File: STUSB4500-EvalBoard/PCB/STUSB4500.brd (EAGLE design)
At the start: 16 x 26 mm, 25 parts

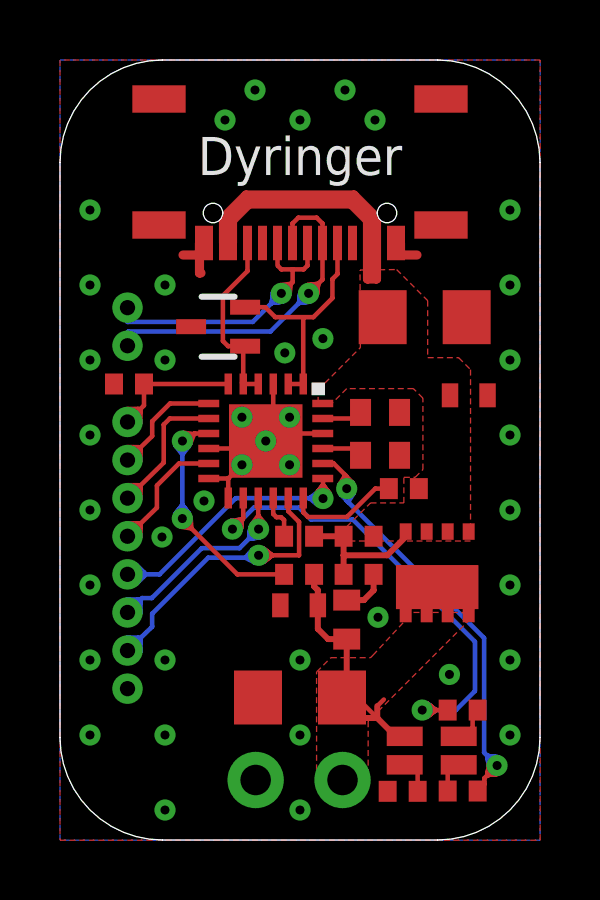
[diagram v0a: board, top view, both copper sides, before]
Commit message: Fixed isolation value on top layer
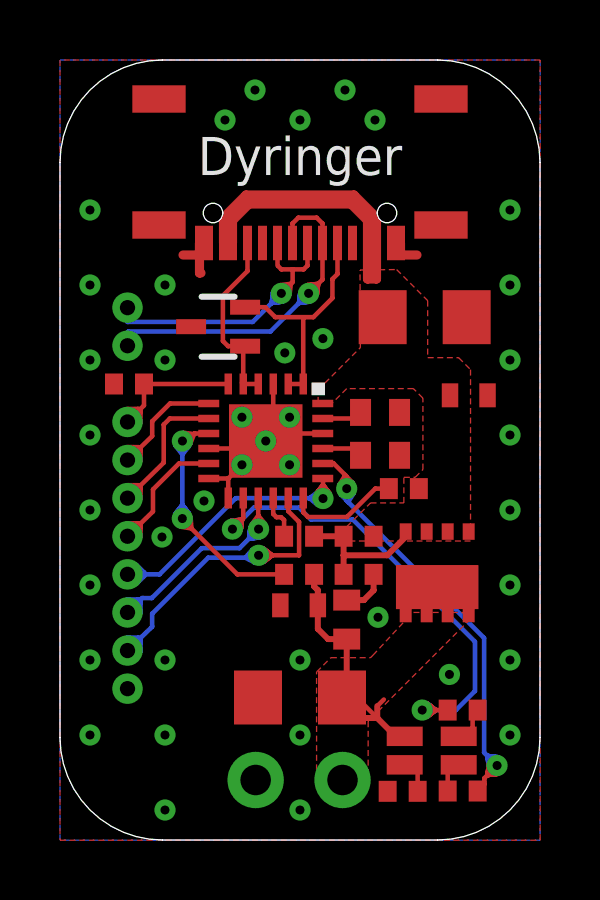
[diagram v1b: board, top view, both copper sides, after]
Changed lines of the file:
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@@
 <wire x1="7.232290625" y1="13.55" x2="7.108125" y2="13.55" width="0.1524" layer="1"/>
 <wire x1="7.108125" y1="15.2" x2="7.108125" y2="13.67416875" width="0.1524" layer="1"/>
-<polygon width="0.1524" layer="1" isolate="0.254" rank="2">
+<polygon width="0.1524" layer="1" isolate="0.1" rank="2">
 <vertex x="0" y="26"/>
 <vertex x="0" y="-0.0075"/>
@@
 <wire x1="7.108125" y1="13.674165625" x2="7.134365625" y2="13.32049375" width="0.1524" layer="1"/>
 <wire x1="6.858125" y1="13.3" x2="7.134365625" y2="13.32049375" width="0.1524" layer="1"/>
-<wire x1="10.5" y1="24" x2="12.7" y2="24.7" width="0" layer="19" extent="1-1"/>
-<wire x1="9.5" y1="25" x2="10.5" y2="24" width="0" layer="19" extent="1-1"/>
-<wire x1="8" y1="24" x2="9.5" y2="25" width="0" layer="19" extent="1-1"/>
-<wire x1="6.5" y1="25" x2="8" y2="24" width="0" layer="19" extent="1-1"/>
-<wire x1="5.5" y1="24" x2="6.5" y2="25" width="0" layer="19" extent="1-1"/>
-<wire x1="3.3" y1="24.7" x2="5.5" y2="24" width="0" layer="19" extent="1-1"/>
-<wire x1="12.7" y1="20.5" x2="10.5" y2="24" width="0" layer="19" extent="1-1"/>
-<wire x1="11.9" y1="19.5" x2="12.7" y2="20.5" width="0" layer="19" extent="1-1"/>
-<wire x1="15" y1="21" x2="12.7" y2="20.5" width="0" layer="19" extent="1-1"/>
-<wire x1="15" y1="18.5" x2="15" y2="21" width="0" layer="19" extent="1-1"/>
-<wire x1="13.555625" y1="17.4275" x2="15" y2="18.5" width="0" layer="19" extent="1-1"/>
-<wire x1="15" y1="16" x2="13.555625" y2="17.4275" width="0" layer="19" extent="1-1"/>
-<wire x1="14.250625" y1="14.8225" x2="15" y2="16" width="0" layer="19" extent="1-1"/>
-<wire x1="15" y1="13.5" x2="14.250625" y2="14.8225" width="0" layer="19" extent="1-1"/>
-<wire x1="15" y1="11" x2="15" y2="13.5" width="0" layer="19" extent="1-1"/>
-<wire x1="15" y1="8.5" x2="15" y2="11" width="0" layer="19" extent="1-1"/>
-<wire x1="15" y1="6" x2="15" y2="8.5" width="0" layer="19" extent="1-1"/>
-<wire x1="12.98125" y1="5.51875" x2="15" y2="6" width="0" layer="19" extent="1-1"/>
-<wire x1="15" y1="3.5" x2="15" y2="6" width="0" layer="19" extent="1-1"/>
-<wire x1="11.318125" y1="14.2525" x2="14.250625" y2="14.8225" width="0" layer="19" extent="1-1"/>
-<wire x1="11.318125" y1="12.82375" x2="11.318125" y2="14.2525" width="0" layer="19" extent="1-1"/>
-<wire x1="8.758125" y1="13.55" x2="11.318125" y2="14.2525" width="0" layer="19" extent="1-1"/>
-<wire x1="6.223125" y1="12.9825" x2="6.608125" y2="13.05" width="0" layer="19" extent="1-1"/>
-<wire x1="6.064375" y1="12.50625" x2="6.223125" y2="12.9825" width="0" layer="19" extent="1-1"/>
-<wire x1="4.8" y1="11.3" x2="4.958125" y2="12.05" width="0" layer="19" extent="1-1"/>
-<wire x1="7.493125" y1="16.236875" x2="7.108125" y2="15.2" width="0" layer="19" extent="1-1"/>
-<wire x1="7.651875" y1="14.09375" x2="6.858125" y2="13.3" width="0" layer="19" extent="1-1"/>
-<wire x1="6.064375" y1="14.09375" x2="6.858125" y2="13.3" width="0" layer="19" extent="1-1"/>
-<wire x1="7.651875" y1="12.50625" x2="6.858125" y2="13.3" width="0" layer="19" extent="1-1"/>
-<wire x1="8.763125" y1="16.713125" x2="7.493125" y2="16.236875" width="0" layer="19" extent="1-1"/>
-<wire x1="3.4" y1="10.1" x2="4.8" y2="11.3" width="0" layer="19" extent="1-1"/>
-<wire x1="1" y1="11" x2="3.4" y2="10.1" width="0" layer="19" extent="1-1"/>
-<wire x1="1" y1="13.5" x2="1" y2="11" width="0" layer="19" extent="1-1"/>
-<wire x1="1.8" y1="15.2" x2="1" y2="13.5" width="0" layer="19" extent="1-1"/>
-<wire x1="1" y1="16" x2="1.8" y2="15.2" width="0" layer="19" extent="1-1"/>
-<wire x1="3.5" y1="16" x2="1.8" y2="15.2" width="0" layer="19" extent="1-1"/>
-<wire x1="4.370625" y1="17.11" x2="3.5" y2="16" width="0" layer="19" extent="1-1"/>
-<wire x1="3.5" y1="18.5" x2="4.370625" y2="17.11" width="0" layer="19" extent="1-1"/>
-<wire x1="4.1" y1="19.5" x2="3.5" y2="18.5" width="0" layer="19" extent="1-1"/>
-<wire x1="3.3" y1="20.5" x2="4.1" y2="19.5" width="0" layer="19" extent="1-1"/>
-<wire x1="1" y1="21" x2="3.3" y2="20.5" width="0" layer="19" extent="1-1"/>
-<wire x1="1" y1="18.5" x2="1" y2="16" width="0" layer="19" extent="1-1"/>
-<wire x1="1" y1="8.5" x2="1" y2="11" width="0" layer="19" extent="1-1"/>
-<wire x1="1" y1="6" x2="1" y2="8.5" width="0" layer="19" extent="1-1"/>
-<wire x1="2.25" y1="5.045" x2="1" y2="6" width="0" layer="19" extent="1-1"/>
-<wire x1="3.5" y1="6" x2="2.25" y2="5.045" width="0" layer="19" extent="1-1"/>
-<wire x1="3.5" y1="3.5" x2="2.25" y2="5.045" width="0" layer="19" extent="1-1"/>
-<wire x1="1" y1="3.5" x2="2.25" y2="5.045" width="0" layer="19" extent="1-1"/>
-<wire x1="3.5" y1="1" x2="3.5" y2="3.5" width="0" layer="19" extent="1-1"/>
-<wire x1="10.6" y1="7.42375" x2="12.98125" y2="5.51875" width="0" layer="19" extent="1-1"/>
-<wire x1="8" y1="6" x2="10.6" y2="7.42375" width="0" layer="19" extent="1-1"/>
-<wire x1="6.6" y1="4.75" x2="8" y2="6" width="0" layer="19" extent="1-1"/>
-<wire x1="8" y1="3.5" x2="6.6" y2="4.75" width="0" layer="19" extent="1-1"/>
-<wire x1="7.344375" y1="7.823125" x2="8" y2="6" width="0" layer="19" extent="1-1"/>
-<wire x1="6.521575" y1="2" x2="8" y2="3.5" width="0" layer="19" extent="1-1"/>
-<wire x1="8" y1="1" x2="6.521575" y2="2" width="0" layer="19" extent="1-1"/>
-<wire x1="10.921875" y1="1.6225" x2="8" y2="1" width="0" layer="19" extent="1-1"/>
+<wire x1="6.608125" y1="13.05" x2="6.223125" y2="12.9825" width="0" layer="19" extent="1-1"/>
 </signal>
 <signal name="STUSB_RST">
@@
 <wire x1="10.55" y1="18.7" x2="10.55" y2="19.9" width="0.3048" layer="1"/>
 <wire x1="10.25" y1="18.7" x2="10.55" y2="18.7" width="0.3048" layer="1"/>
-<wire x1="11.961875" y1="11.7125" x2="13.000625" y2="14.8225" width="0" layer="19" extent="1-1"/>
-<wire x1="12.223125" y1="10.28125" x2="11.961875" y2="11.7125" width="0" layer="19" extent="1-1"/>
-<wire x1="12.923125" y1="10.28125" x2="12.223125" y2="10.28125" width="0" layer="19" extent="1-1"/>
-<wire x1="13.623125" y1="10.28125" x2="12.923125" y2="10.28125" width="0" layer="19" extent="1-1"/>
-<wire x1="10.45375" y1="10.125" x2="12.223125" y2="10.28125" width="0" layer="19" extent="1-1"/>
-<wire x1="10.755625" y1="17.4275" x2="13.000625" y2="14.8225" width="0" layer="19" extent="1-1"/>
-<wire x1="10.25" y1="19.9" x2="10.419375" y2="17.4275" width="0" layer="19" extent="1-1"/>
-<wire x1="8.758125" y1="14.55" x2="10.119375" y2="17.4275" width="0" layer="19" extent="1-1"/>
 </signal>
 <signal name="N$5">
@@
 <wire x1="10.57515625" y1="4.06640625" x2="9.82421875" y2="4.06640625" width="0.2" layer="1"/>
 <wire x1="9.82421875" y1="4.06640625" x2="9.763125" y2="4.1275" width="0.1524" layer="1"/>
-<wire x1="12.923125" y1="7.53125" x2="13.623125" y2="7.53125" width="0" layer="19" extent="1-1"/>
-<wire x1="12.223125" y1="7.53125" x2="12.923125" y2="7.53125" width="0" layer="19" extent="1-1"/>
-<wire x1="11.523125" y1="7.53125" x2="12.223125" y2="7.53125" width="0" layer="19" extent="1-1"/>
-<wire x1="9.556875" y1="6.696875" x2="11.523125" y2="7.53125" width="0" layer="19" extent="1-1"/>
-<wire x1="10.08875" y1="4.5528125" x2="9.4" y2="4.75" width="0" layer="19" extent="1-1"/>
-<wire x1="9.417175" y1="2" x2="9.763125" y2="4.1275" width="0" layer="19" extent="1-1"/>
 </signal>
 <signal name="N$14">
@@
 <contactref element="U$1" pad="11"/>
 <wire x1="4.958125" y1="12.55" x2="3.9649125" y2="12.55" width="0.1524" layer="1"/>
-<wire x1="3.9649125" y1="12.55" x2="3.230625" y2="11.8157125" width="0.1524" layer="1"/>
-<wire x1="3.230625" y1="11.8157125" x2="3.230625" y2="11.0775" width="0.1524" layer="1"/>
+<wire x1="3.9649125" y1="12.55" x2="3.099453125" y2="11.684540625" width="0.1524" layer="1"/>
+<wire x1="3.099453125" y1="11.684540625" x2="3.099453125" y2="10.950090625" width="0.1524" layer="1"/>
 <contactref element="J8" pad="4"/>
-<wire x1="3.230625" y1="11.0775" x2="2.6144" y2="10.478946875" width="0.1524" layer="1"/>
+<wire x1="3.099453125" y1="10.950090625" x2="2.6144" y2="10.478946875" width="0.1524" layer="1"/>
 <wire x1="2.6144" y1="10.478946875" x2="2.25" y2="10.125" width="0.1524" layer="1"/>
 <wire x1="2.6144" y1="10.478946875" x2="2.25161875" y2="10.480596875" width="0.3048" layer="1"/>

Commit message: Cleanups in  stusb4500 eval
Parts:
- moved R3 0.13 mm to (13.3, 1.63)
- moved R2 0.07 mm to (11.5, 1.62)
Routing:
- net USB_D+: track 14.3 -> 15.0 mm
- net USB_D-: track 17.6 -> 18.3 mm

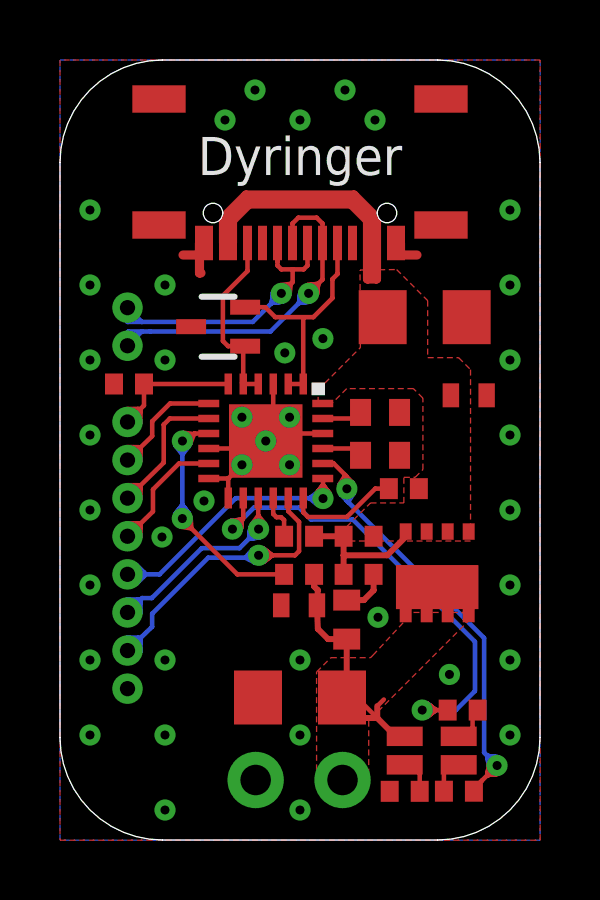
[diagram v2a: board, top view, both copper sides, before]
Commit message: Unified 0402 footprint, reduced height of stusb4500 eval board to 24mm
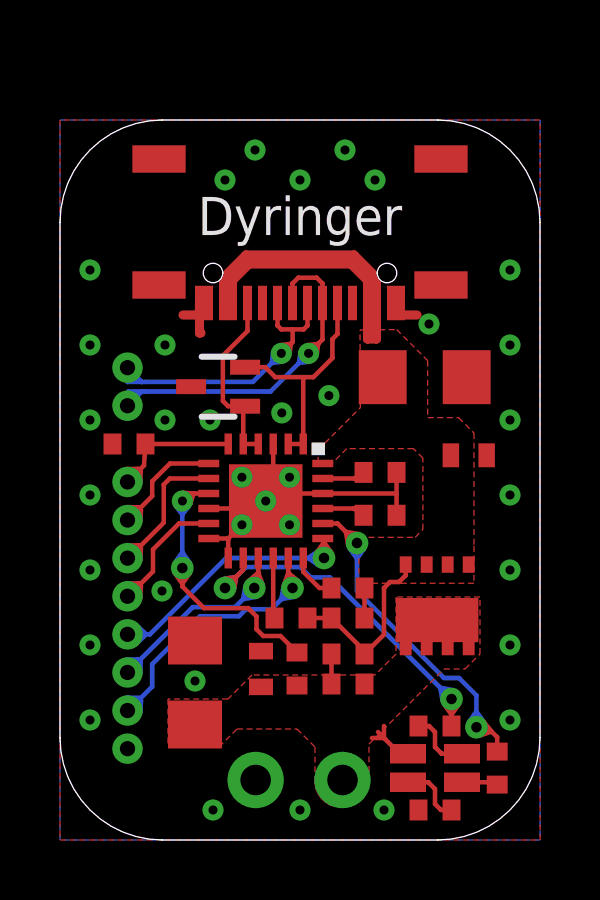
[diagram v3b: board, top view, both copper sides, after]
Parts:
- moved R7 3.80 mm to (9.60, 8.40)
- moved C5 3.54 mm to (4.50, 5.25), turned to 90 degrees
- moved R10 3.16 mm to (7.90, 5.70), turned to 90 degrees
- moved R4 2.75 mm to (9.60, 7.40)
- moved R5 2.74 mm to (7.70, 7.40)
- moved R6 2.68 mm to (9.60, 6.20), turned to 0 degrees
- moved U$5 2.47 mm to (6.70, 5.70), turned to 90 degrees
- moved C3 2.15 mm to (9.60, 5.20), turned to 0 degrees
- moved J6 2.00 mm to (2.25, 15.7)
- moved C1 2.00 mm to (10.7, 12.3)
- moved C2 2.00 mm to (10.7, 10.8)
- moved ESDA25W 2.00 mm to (5.27, 15.1)
- moved J5 2.00 mm to (2.25, 5.58)
- moved J8 2.00 mm to (2.25, 11.9)
- moved R1 2.00 mm to (2.30, 13.2)
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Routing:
- net STUSB_PDO3: track 28.2 -> 17.7 mm
- net USB_PD_VDD: track 9.41 -> 2.10 mm
- net GND: track 18.2 -> 24.9 mm, vias 40 -> 35
- net STUSB_PDO2: track 23.2 -> 16.7 mm
- net USB_D-: track 18.3 -> 14.6 mm
- net N$5: track 3.79 -> 1.63 mm
- net STUSB_AB: track 15.2 -> 13.1 mm
- net USB_D+: track 15.0 -> 13.0 mm
- net STUSB_GPIO: track 12.5 -> 10.9 mm
- net STUSB_ALERT: track 14.2 -> 12.6 mm
- net N$3: track 4.75 -> 6.18 mm
- net VDD: track 18.0 -> 19.0 mm
- net N$20: track 1.24 -> 2.13 mm
- net N$2: track 1.32 -> 2.13 mm
- net N$7: track 1.56 -> 1.00 mm
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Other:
- board size 16 x 26 mm -> 16 x 24 mm
